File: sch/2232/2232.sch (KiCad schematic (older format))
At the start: 58 parts

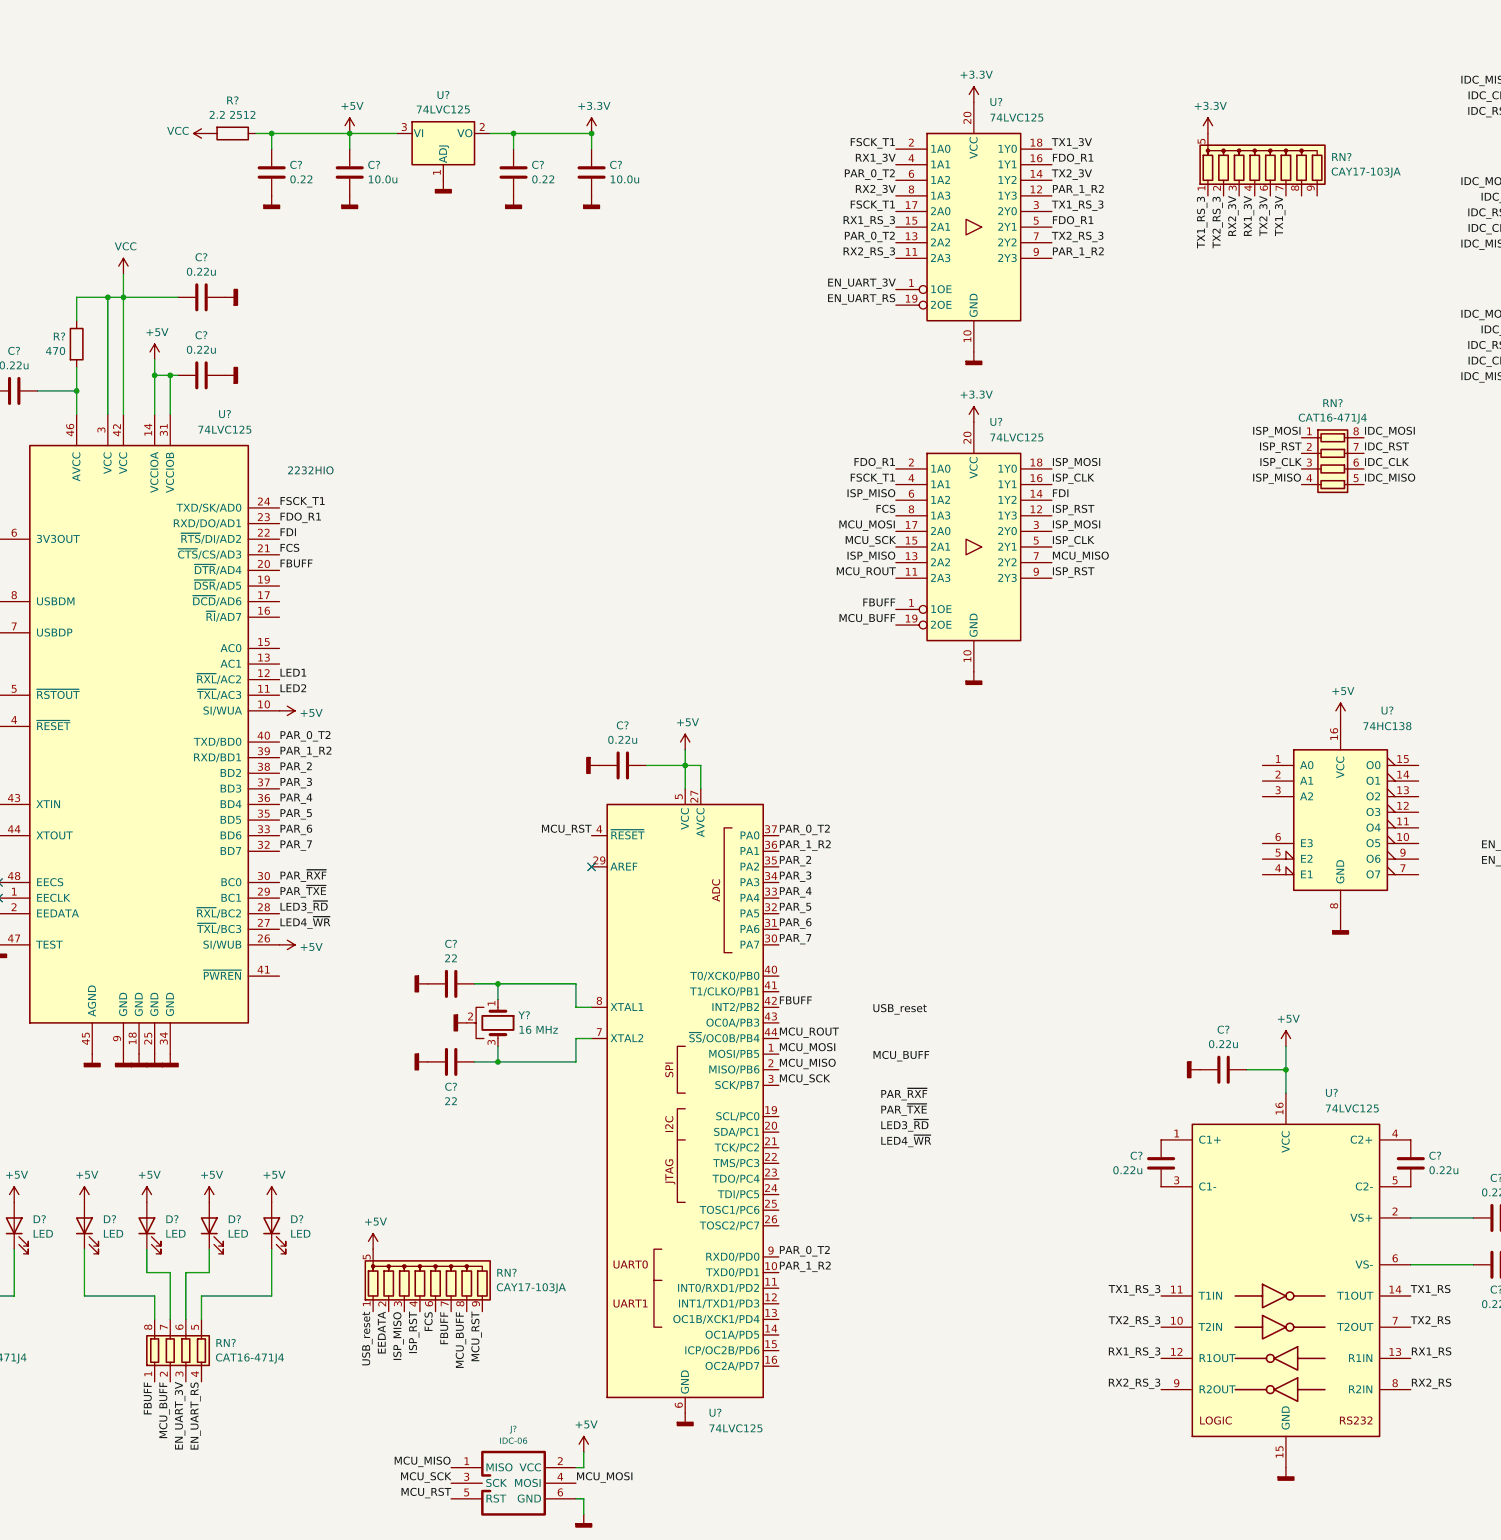
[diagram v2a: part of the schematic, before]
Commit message: Names fixed. Footprints assigned
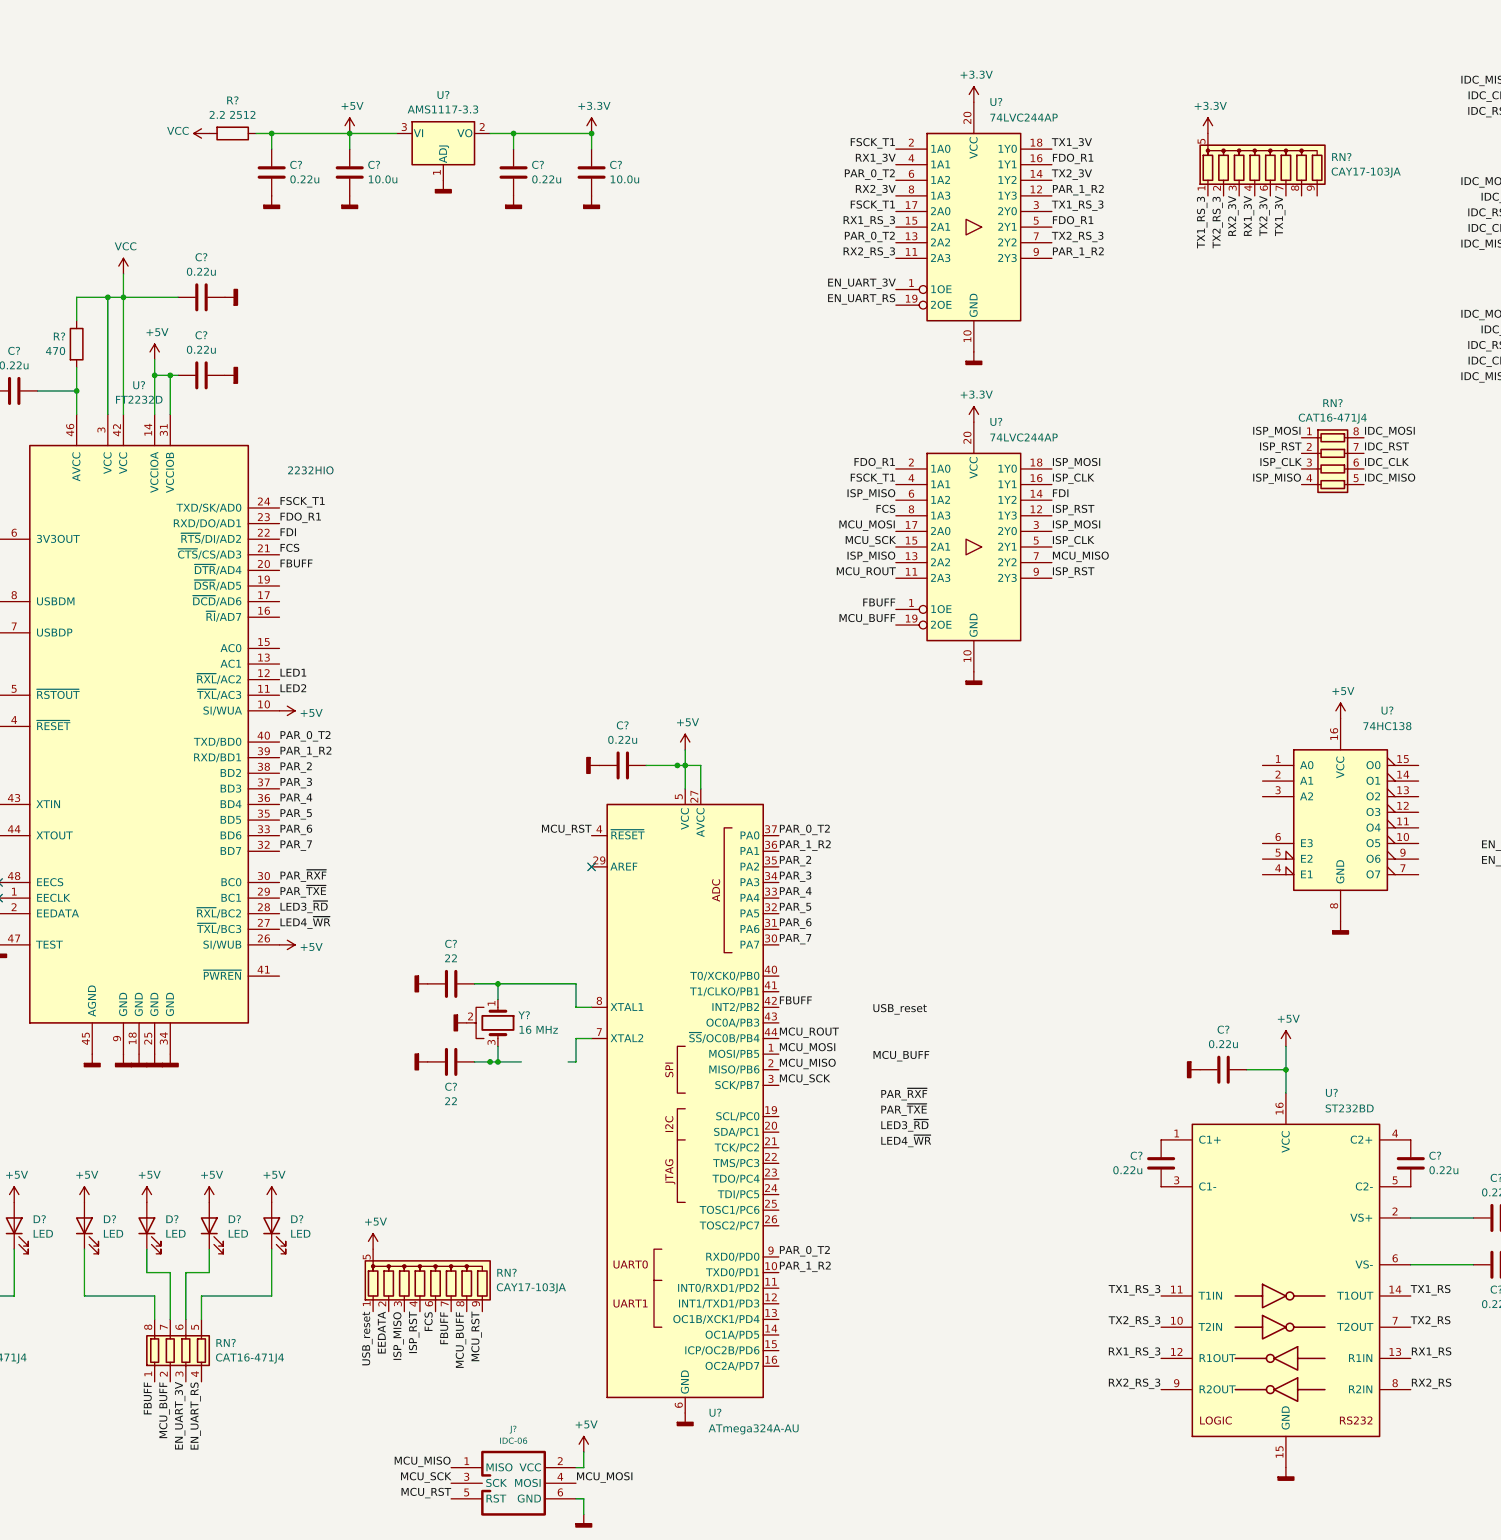
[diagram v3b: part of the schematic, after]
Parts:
- removed U?: 74LVC125, symbol symbol:FT2232D
- added U?: FT2232D, NevaDA:LQFP-48_7x7mm_P0.5mm, symbol symbol:FT2232D
- C? (x15): footprint (none) -> NevaDA:C_0603
- C? (x2): value 0.22 -> 0.22u; footprint (none) -> NevaDA:C_0603
- C? (x2): footprint (none) -> NevaDA:C_1206
- J? (x2): footprint (none) -> NevaDA:Terminal_3.5mm_x6
- R? (x4): footprint (none) -> NevaDA:R_0603
- R?: footprint (none) -> NevaDA:R_2512
- RN? (x5): footprint (none) -> NevaDA:R_CAT-16-4
- U?: value 74LVC125 -> AMS1117-3.3; footprint (none) -> NevaDA:SOT-223
- U?: value 74LVC125 -> ATmega324A-AU; footprint (none) -> NevaDA:TQFP-44
- U? (x2): value 74LVC125 -> 74LVC244AP; footprint (none) -> NevaDA:TSSOP-20
- U?: value 74LVC125 -> ST232BD; footprint (none) -> NevaDA:SOIC-16
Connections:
- net +5V: now also U?.10 (SI/WUA), U?.14 (VCCIOA), U?.26 (SI/WUB), U?.31 (VCCIOB)
- net EEDATA: now also U?.2 (EEDATA)
- net FBUFF: now also U?.20 (~DTR~/AD4)
- net FCS: now also U?.21 (~CTS~/CS/AD3)
- net FDI: now also U?.22 (~RTS~/DI/AD2)
- net FDO_R1: now also U?.23 (RXD/DO/AD1)
- net FSCK_T1: now also U?.24 (TXD/SK/AD0)
- net GNDD: now also U?.18 (GND), U?.25 (GND), U?.34 (GND), U?.45 (AGND), U?.47 (TEST), U?.9 (GND)
- net LED1: now also U?.12 (~RXL~/AC2)
- net LED2: now also U?.11 (~TXL~/AC3)
- net LED3_~RD: now also U?.28 (~RXL~/BC2)
- net LED4_~WR: now also U?.27 (~TXL~/BC3)
- net PAR_0_T2: now also U?.40 (TXD/BD0)
- net PAR_1_R2: now also U?.39 (RXD/BD1)
- net PAR_2: now also U?.38 (BD2)
- net PAR_3: now also U?.37 (BD3)
- net PAR_4: now also U?.36 (BD4)
- net PAR_5: now also U?.35 (BD5)
- net PAR_6: now also U?.33 (BD6)
- net PAR_7: now also U?.32 (BD7)
- net PAR_~RXF: now also U?.30 (BC0)
- net PAR_~TXE: now also U?.29 (BC1)
- net USB_reset: now also U?.4 (~RESET)
- net USBf_m: now also U?.8 (USBDM)
- net USBf_p: now also U?.7 (USBDP)
- net VCC: now also U?.3 (VCC), U?.42 (VCC)
- net at C?.1, Y?.1: now also U?.43 (XTIN)
- net at C?.1, Y?.3: now also U?.44 (XTOUT)
- net at C?.1, R?.2: now also U?.46 (AVCC)
- net at R?.1: now also U?.5 (~RSTOUT)
- net at C?.1: now also U?.6 (3V3OUT)
- net at C?.1, Y?.3: no longer U?.7 (XTAL2)
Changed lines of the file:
@@
 $EndDescr
-$Comp
-L symbol:FT2232D U?
-U 1 1 5FD3B071
-P 3400 5550
-F 0 "U?" H 3950 7650 50  0000 C CNN
-F 1 "74LVC125" H 3950 7550 50  0000 C CNN
-F 2 "" H 3400 5550 50  0001 C CNN
-F 3 "http://www.ti.com/lit/gpn/sn74LVC125" H 3400 5550 50  0001 C CNN
-	1    3400 5550
-	1    0    0    -1
-$EndComp
 $Comp
 L Connector:6P6C J?
@@
 P 5350 1650
 F 0 "U?" H 5350 1895 50  0000 C CNN
-F 1 "74LVC125" H 5350 1802 50  0000 C CNN
-F 2 "" H 5350 1900 50  0001 C CIN
+F 1 "AMS1117-3.3" H 5350 1802 50  0000 C CNN
+F 2 "NevaDA:SOT-223" H 5350 1900 50  0001 C CIN
 F 3 "http://www.ti.com/lit/gpn/sn74LVC125" H 5350 1650 50  0001 C CNN
 	1    5350 1650
@@
 P 6900 7850
 F 0 "U?" H 7050 5850 50  0000 L CNN
-F 1 "74LVC125" H 7050 5750 50  0000 L CNN
-F 2 "" H 6900 7850 50  0001 C CIN
-F 3 "http://www.ti.com/lit/gpn/sn74LVC125" H 6900 7850 50  0001 C CNN
+F 1 "ATmega324A-AU" H 7050 5750 50  0000 L CNN
+F 2 "NevaDA:TQFP-44" H 6900 7850 50  0001 C CIN
+F 3 "" H 6900 7850 50  0001 C CNN
 	1    6900 7850
 	1    0    0    -1
@@
 P 10750 9000
 F 0 "U?" H 11000 10200 50  0000 L CNN
-F 1 "74LVC125" H 11000 10100 50  0000 L CNN
-F 2 "" H 10800 7950 50  0001 L CNN
-F 3 "http://www.ti.com/lit/gpn/sn74LVC125" H 10750 9100 50  0001 C CNN
+F 1 "ST232BD" H 11000 10100 50  0000 L CNN
+F 2 "NevaDA:SOIC-16" H 10800 7950 50  0001 L CNN
+F 3 "" H 10750 9100 50  0001 C CNN
 	1    10750 9000
 	1    0    0    -1
@@
 F 0 "R?" V 1190 4800 50  0000 C CNN
 F 1 "27" V 1283 4800 50  0000 C CNN
-F 2 "" V 1330 4800 50  0001 C CNN
+F 2 "NevaDA:R_0603" V 1330 4800 50  0001 C CNN
 F 3 "~" H 1400 4800 50  0001 C CNN
 	1    1400 4800
@@
 F 0 "R?" H 2931 3047 50  0000 R CNN
 F 1 "470" H 2931 2954 50  0000 R CNN
-F 2 "" V 2930 3000 50  0001 C CNN
+F 2 "NevaDA:R_0603" V 2930 3000 50  0001 C CNN
 F 3 "~" H 3000 3000 50  0001 C CNN
 	1    3000 3000
@@
 F 0 "C?" V 2345 3300 50  0000 C CNN
 F 1 "0.22u" V 2438 3300 50  0000 C CNN
-F 2 "" H 2638 3150 50  0001 C CNN
+F 2 "NevaDA:C_0603" H 2638 3150 50  0001 C CNN
 F 3 "~" H 2600 3300 50  0001 C CNN
 	1    2600 3300
@@
 F 0 "R?" V 1190 4450 50  0000 C CNN
 F 1 "27" V 1283 4450 50  0000 C CNN
-F 2 "" V 1330 4450 50  0001 C CNN
+F 2 "NevaDA:R_0603" V 1330 4450 50  0001 C CNN
 F 3 "~" H 1400 4450 50  0001 C CNN
 	1    1400 4450
@@
 F 0 "C?" V 2095 4250 50  0000 C CNN
 F 1 "0.22u" V 2188 4250 50  0000 C CNN
-F 2 "" H 2388 4100 50  0001 C CNN
+F 2 "NevaDA:C_0603" H 2388 4100 50  0001 C CNN
 F 3 "~" H 2350 4250 50  0001 C CNN
 	1    2350 4250
@@
 F 0 "C?" V 1295 5800 50  0000 C CNN
 F 1 "22" V 1388 5800 50  0000 C CNN
-F 2 "" H 1588 5650 50  0001 C CNN
+F 2 "NevaDA:C_0603" H 1588 5650 50  0001 C CNN
 F 3 "~" H 1550 5800 50  0001 C CNN
 	1    1550 5800
@@
 F 0 "C?" V 1711 6300 50  0000 C CNN
 F 1 "22" V 1804 6300 50  0000 C CNN
-F 2 "" H 1588 6150 50  0001 C CNN
+F 2 "NevaDA:C_0603" H 1588 6150 50  0001 C CNN
 F 3 "~" H 1550 6300 50  0001 C CNN
 	1    1550 6300
@@
 F 0 "C?" V 4055 2700 50  0000 C CNN
 F 1 "0.22u" V 3962 2700 50  0000 C CNN
-F 2 "" H 3838 2550 50  0001 C CNN
+F 2 "NevaDA:C_0603" H 3838 2550 50  0001 C CNN
 F 3 "~" H 3800 2700 50  0001 C CNN
 	1    3800 2700
@@
 F 0 "R?" V 2140 5250 50  0000 C CNN
 F 1 "1.5k" V 2233 5250 50  0000 C CNN
-F 2 "" V 2280 5250 50  0001 C CNN
+F 2 "NevaDA:R_0603" V 2280 5250 50  0001 C CNN
 F 3 "~" H 2350 5250 50  0001 C CNN
 	1    2350 5250
@@
 P 8750 2250
 F 0 "U?" H 8850 3050 50  0000 L CNN
-F 1 "74LVC125" H 8850 2950 50  0000 L CNN
-F 2 "" H 8750 2250 50  0001 C CNN
+F 1 "74LVC244AP" H 8850 2950 50  0000 L CNN
+F 2 "NevaDA:TSSOP-20" H 8750 2250 50  0001 C CNN
 F 3 "http://www.ti.com/lit/gpn/sn74LVC125" H 8750 2250 50  0001 C CNN
 	1    8750 2250
@@
 F 0 "R?" V 3790 1650 50  0000 C CNN
 F 1 "2.2 2512" V 3883 1650 50  0000 C CNN
-F 2 "" V 3930 1650 50  0001 C CNN
+F 2 "NevaDA:R_2512" V 3930 1650 50  0001 C CNN
 F 3 "~" H 4000 1650 50  0001 C CNN
 	1    4000 1650
@@
 P 4250 1900
 F 0 "C?" H 4365 1947 50  0000 L CNN
-F 1 "0.22" H 4365 1854 50  0000 L CNN
-F 2 "" H 4288 1750 50  0001 C CNN
+F 1 "0.22u" H 4365 1854 50  0000 L CNN
+F 2 "NevaDA:C_0603" H 4288 1750 50  0001 C CNN
 F 3 "~" H 4250 1900 50  0001 C CNN
 	1    4250 1900
@@
 F 0 "C?" H 4865 1947 50  0000 L CNN
 F 1 "10.0u" H 4865 1854 50  0000 L CNN
-F 2 "" H 4788 1750 50  0001 C CNN
+F 2 "NevaDA:C_1206" H 4788 1750 50  0001 C CNN
 F 3 "~" H 4750 1900 50  0001 C CNN
 	1    4750 1900
@@
 P 5800 1900
 F 0 "C?" H 5915 1947 50  0000 L CNN
-F 1 "0.22" H 5915 1854 50  0000 L CNN
-F 2 "" H 5838 1750 50  0001 C CNN
+F 1 "0.22u" H 5915 1854 50  0000 L CNN
+F 2 "NevaDA:C_0603" H 5838 1750 50  0001 C CNN
 F 3 "~" H 5800 1900 50  0001 C CNN
 	1    5800 1900
@@
 F 0 "C?" H 6415 1947 50  0000 L CNN
 F 1 "10.0u" H 6415 1854 50  0000 L CNN
-F 2 "" H 6338 1750 50  0001 C CNN
+F 2 "NevaDA:C_1206" H 6338 1750 50  0001 C CNN
 F 3 "~" H 6300 1900 50  0001 C CNN
 	1    6300 1900
@@
 F 0 "C?" V 4055 3200 50  0000 C CNN
 F 1 "0.22u" V 3962 3200 50  0000 C CNN
-F 2 "" H 3838 3050 50  0001 C CNN
+F 2 "NevaDA:C_0603" H 3838 3050 50  0001 C CNN
 F 3 "~" H 3800 3200 50  0001 C CNN
 	1    3800 3200
@@
 P 8750 4300
 F 0 "U?" H 8850 5100 50  0000 L CNN
-F 1 "74LVC125" H 8850 5000 50  0000 L CNN
-F 2 "" H 8750 4300 50  0001 C CNN
+F 1 "74LVC244AP" H 8850 5000 50  0000 L CNN
+F 2 "NevaDA:TSSOP-20" H 8750 4300 50  0001 C CNN
 F 3 "http://www.ti.com/lit/gpn/sn74LVC125" H 8750 4300 50  0001 C CNN
 	1    8750 4300
@@
 	5700 7100 6200 7100
 Wire Wire Line
-	5700 7600 6200 7600
+	5700 7600 5850 7600
 Wire Wire Line
 	5700 7500 5700 7600
@@
 F 0 "C?" V 5145 7100 50  0000 C CNN
 F 1 "22" V 5238 7100 50  0000 C CNN
-F 2 "" H 5438 6950 50  0001 C CNN
+F 2 "NevaDA:C_0603" H 5438 6950 50  0001 C CNN
 F 3 "~" H 5400 7100 50  0001 C CNN
 	1    5400 7100
@@
 F 0 "C?" V 5561 7600 50  0000 C CNN
 F 1 "22" V 5654 7600 50  0000 C CNN
-F 2 "" H 5438 7450 50  0001 C CNN
+F 2 "NevaDA:C_0603" H 5438 7450 50  0001 C CNN
 F 3 "~" H 5400 7600 50  0001 C CNN
 	1    5400 7600
@@
 Connection ~ 5700 7100
 Wire Wire Line
-	5550 7600 5700 7600
+	5550 7600 5650 7600
 Connection ~ 5700 7600
 Wire Wire Line
@@
 F 0 "J?" H 15030 5096 50  0000 L CNN
 F 1 "Screw_Terminal_01x06" H 15030 5050 50  0001 L CNN
-F 2 "" H 14950 5150 50  0001 C CNN
+F 2 "NevaDA:Terminal_3.5mm_x6" H 14950 5150 50  0001 C CNN
 F 3 "~" H 14950 5150 50  0001 C CNN
 	1    14950 5150
@@
 F 0 "J?" H 15030 6446 50  0000 L CNN
 F 1 "Screw_Terminal_01x06" H 15030 6400 50  0001 L CNN
-F 2 "" H 14950 6500 50  0001 C CNN
+F 2 "NevaDA:Terminal_3.5mm_x6" H 14950 6500 50  0001 C CNN
 F 3 "~" H 14950 6500 50  0001 C CNN
 	1    14950 6500
@@
 F 0 "RN?" V 13480 5250 50  0000 C CNN
 F 1 "CAT16-471J4" V 13573 5250 50  0000 C CNN
-F 2 "" V 14175 5250 50  0001 C CNN
+F 2 "NevaDA:R_CAT-16-4" V 14175 5250 50  0001 C CNN
 F 3 "~" H 13900 5250 50  0001 C CNN
 	1    13900 5250
@@
 F 0 "RN?" V 13480 6600 50  0000 C CNN
 F 1 "CAT16-471J4" V 13573 6600 50  0000 C CNN
-F 2 "" V 14175 6600 50  0001 C CNN
+F 2 "NevaDA:R_CAT-16-4" V 14175 6600 50  0001 C CNN
 F 3 "~" H 13900 6600 50  0001 C CNN
 	1    13900 6600
@@
 F 0 "C?" V 13795 3200 50  0000 C CNN
 F 1 "0.22u" V 13888 3200 50  0000 C CNN
-F 2 "" H 14088 3050 50  0001 C CNN
+F 2 "NevaDA:C_0603" H 14088 3050 50  0001 C CNN
 F 3 "~" H 14050 3200 50  0001 C CNN
 	1    14050 3200
@@
 F 0 "C?" H 9835 8297 50  0000 R CNN
 F 1 "0.22u" H 9835 8204 50  0000 R CNN
-F 2 "" H 9988 8100 50  0001 C CNN
+F 2 "NevaDA:C_0603" H 9988 8100 50  0001 C CNN
 F 3 "~" H 9950 8250 50  0001 C CNN
 	1    9950 8250
@@
 F 0 "C?" H 11665 8297 50  0000 L CNN
 F 1 "0.22u" H 11665 8204 50  0000 L CNN
-F 2 "" H 11588 8100 50  0001 C CNN
+F 2 "NevaDA:C_0603" H 11588 8100 50  0001 C CNN
 F 3 "~" H 11550 8250 50  0001 C CNN
 	1    11550 8250
@@
 F 0 "C?" V 12261 8900 50  0000 C CNN
 F 1 "0.22u" V 12354 8900 50  0000 C CNN
-F 2 "" H 12138 8750 50  0001 C CNN
+F 2 "NevaDA:C_0603" H 12138 8750 50  0001 C CNN
 F 3 "~" H 12100 8900 50  0001 C CNN
 	1    12100 8900
@@
 F 0 "C?" V 11845 8600 50  0000 C CNN
 F 1 "0.22u" V 11938 8600 50  0000 C CNN
-F 2 "" H 12138 8450 50  0001 C CNN
+F 2 "NevaDA:C_0603" H 12138 8450 50  0001 C CNN
 F 3 "~" H 12100 8600 50  0001 C CNN
 	1    12100 8600
@@
 F 0 "C?" V 10605 7650 50  0000 C CNN
 F 1 "0.22u" V 10512 7650 50  0000 C CNN
-F 2 "" H 10388 7500 50  0001 C CNN
+F 2 "NevaDA:C_0603" H 10388 7500 50  0001 C CNN
 F 3 "~" H 10350 7650 50  0001 C CNN
 	1    10350 7650
@@
 F 0 "RN?" V 10630 3800 50  0000 C CNN
 F 1 "CAT16-471J4" V 10723 3800 50  0000 C CNN
-F 2 "" V 11325 3800 50  0001 C CNN
+F 2 "NevaDA:R_CAT-16-4" V 11325 3800 50  0001 C CNN
 F 3 "~" H 11050 3800 50  0001 C CNN
 	1    11050 3800
@@
 F 0 "C?" V 6245 5700 50  0000 C CNN
 F 1 "0.22u" V 6338 5700 50  0000 C CNN
-F 2 "" H 6538 5550 50  0001 C CNN
+F 2 "NevaDA:C_0603" H 6538 5550 50  0001 C CNN
 F 3 "~" H 6500 5700 50  0001 C CNN
 	1    6500 5700
@@
 $EndComp
 Wire Wire Line
-	6650 5700 6900 5700
+	6650 5700 6850 5700
 $Comp
 L power:+5V #PWR?
@@
 F 0 "RN?" H 2239 9497 50  0000 L CNN
 F 1 "CAT16-471J4" H 2239 9404 50  0000 L CNN
-F 2 "" V 2325 9450 50  0001 C CNN
+F 2 "NevaDA:R_CAT-16-4" V 2325 9450 50  0001 C CNN
 F 3 "~" H 2050 9450 50  0001 C CNN
 	1    2050 9450
@@
 F 0 "RN?" H 3889 9497 50  0000 L CNN
 F 1 "CAT16-471J4" H 3889 9404 50  0000 L CNN
-F 2 "" V 3975 9450 50  0001 C CNN
+F 2 "NevaDA:R_CAT-16-4" V 3975 9450 50  0001 C CNN
 F 3 "~" H 3700 9450 50  0001 C CNN
 	1    3700 9450
@@
 	1    0    0    -1
 $EndComp
+$Comp
+L symbol:FT2232D U?
+U 1 1 5FD8C583
+P 3400 5550
+F 0 "U?" H 3400 7835 50  0000 C CNN
+F 1 "FT2232D" H 3400 7742 50  0000 C CNN
+F 2 "NevaDA:LQFP-48_7x7mm_P0.5mm" H 3400 5550 50  0001 C CNN
+F 3 "http://www.intersil.com/content/dam/Intersil/documents/icl3/icl3221-22-23-32-41-43.pdf" H 3400 5550 50  0001 C CNN
+	1    3400 5550
+	1    0    0    -1
+$EndComp
+Wire Wire Line
+	6150 7600 6200 7600
+Connection ~ 6850 5700
+Wire Wire Line
+	6850 5700 6900 5700
+Connection ~ 5650 7600
+Wire Wire Line
+	5650 7600 5700 7600
 $EndSCHEMATC

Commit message: PCB orientation stub
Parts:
- U7: renamed from U?; symbol symbol:74HC138 -> 2232-rescue:74HC138-symbol
- gave numbers to parts that had none: 57
